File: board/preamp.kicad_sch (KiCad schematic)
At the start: 18 parts, among them U5 MAX4062

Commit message: 0.2-prototype
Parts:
- R39: value 220 -> 220-1%
- TP6: now left out of the parts list
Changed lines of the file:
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@@
 		(unit 1)
 		(exclude_from_sim no)
-		(in_bom yes)
+		(in_bom no)
 		(on_board yes)
 		(dnp no)
@@
 			)
 		)
-		(property "Value" "220"
+		(property "Value" "220-1%"
 			(at 222.25 85.09 90)
 			(effects

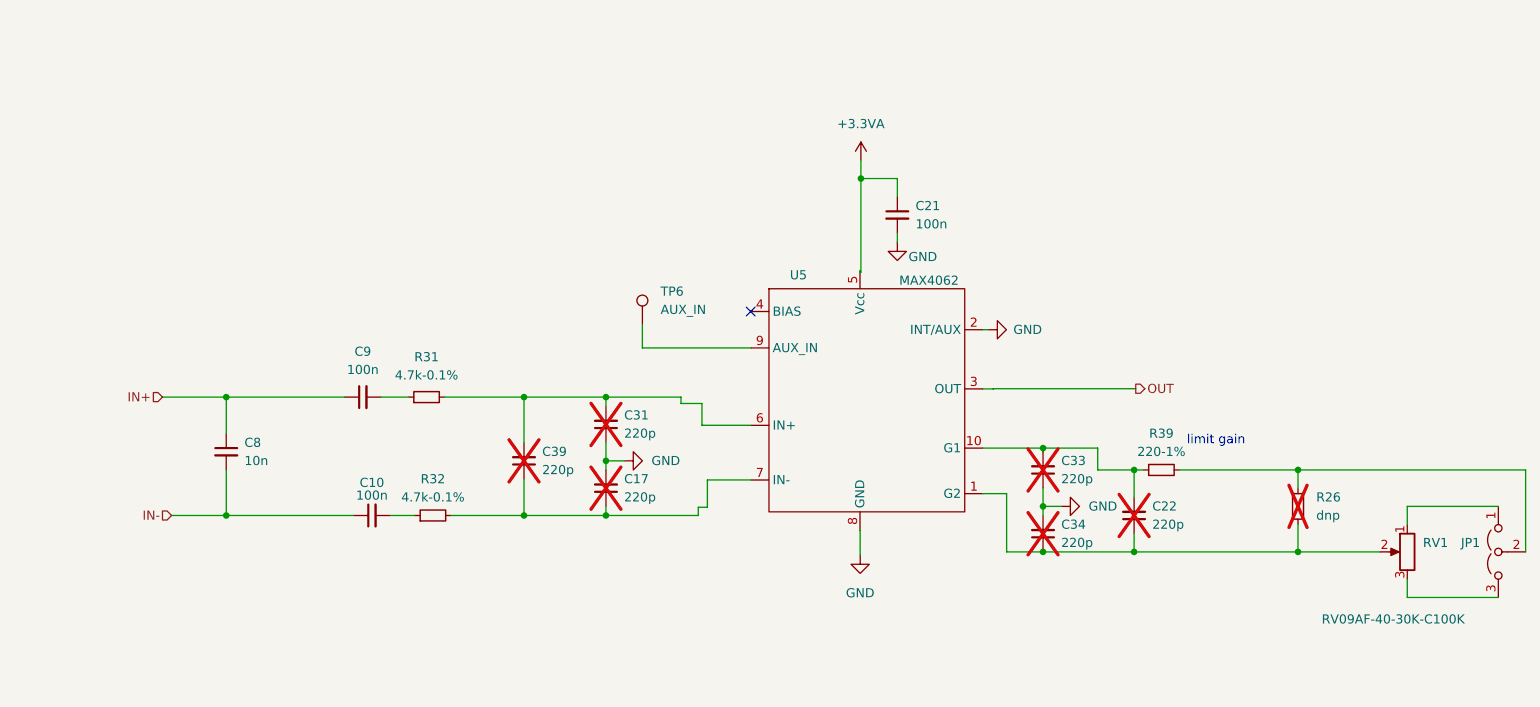
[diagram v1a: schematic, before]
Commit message: redesigned MAX section with shorter traces, analog GND plane,...
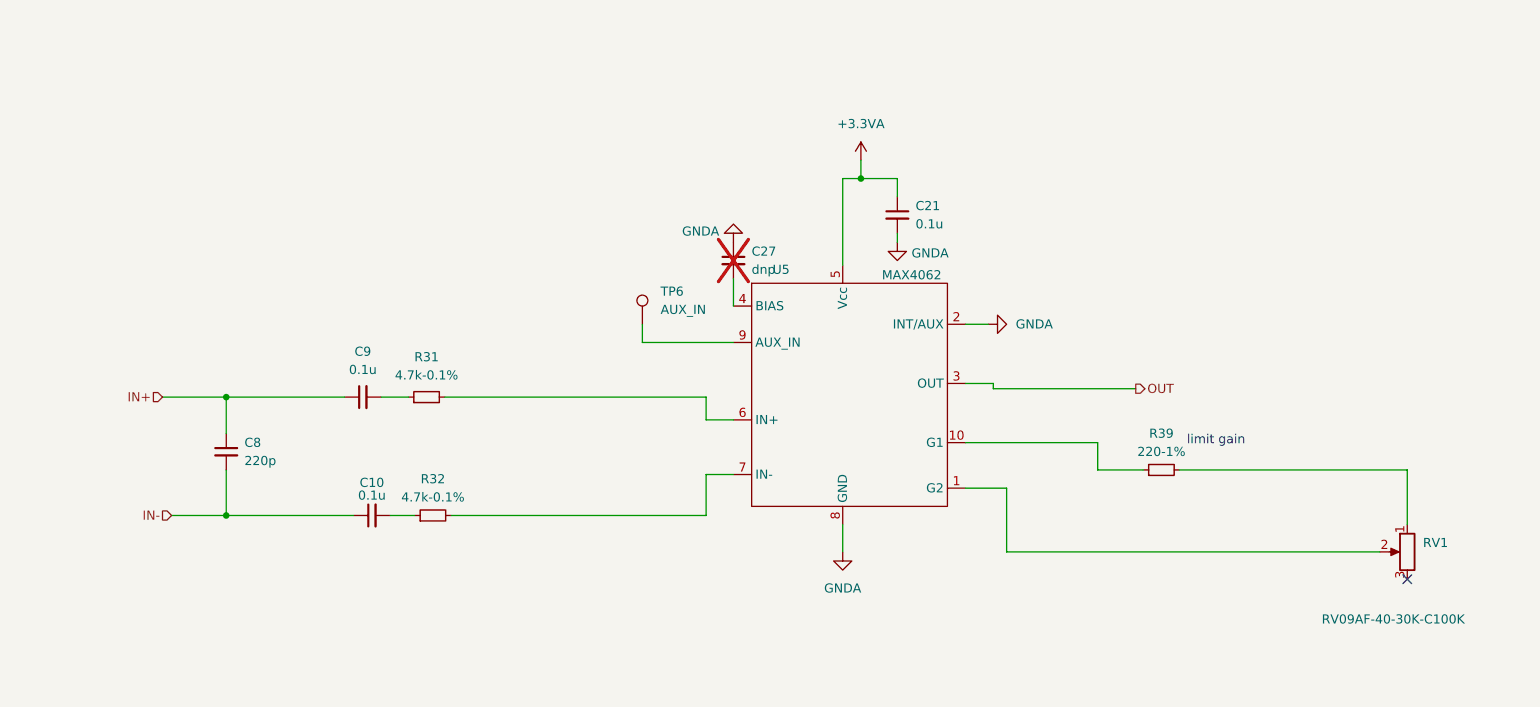
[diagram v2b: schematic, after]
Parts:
- removed C17, C22, C31, C33, C34, C39: 220p, Capacitor_THT:C_Disc_D3.0mm_W2.0mm_P2.50mm, symbol Device:C_Small
- removed JP1: ~, Jumper:SolderJumper-3_P1.3mm_Open_RoundedPad1.0x1.5mm_NumberLabels, symbol Jumper:Jumper_3_Open
- removed R26: dnp, Resistor_THT:R_Axial_DIN0207_L6.3mm_D2.5mm_P10.16mm_Horizontal, symbol Device:R_Small
- added C27: dnp, Capacitor_SMD:C_1206_3216Metric_Pad1.33x1.80mm_HandSolder, symbol Device:C_Small
- C10, C21, C9: value 100n -> 0.1u
- C8: value 10n -> 220p; footprint Capacitor_THT:C_Disc_D5.1mm_W3.2mm_P5.00mm -> Capacitor_THT:C_Disc_D3.0mm_W2.0mm_P2.50mm
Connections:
- net at R39.2: now also RV1.1
- net at U5.4 (BIAS): now also C27.2
- net GND renamed GNDA
- net GNDA: now also C27.1
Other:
- moved on the sheet: U5

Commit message: revert separating ground planes
maybe it leads to more issues than it solves
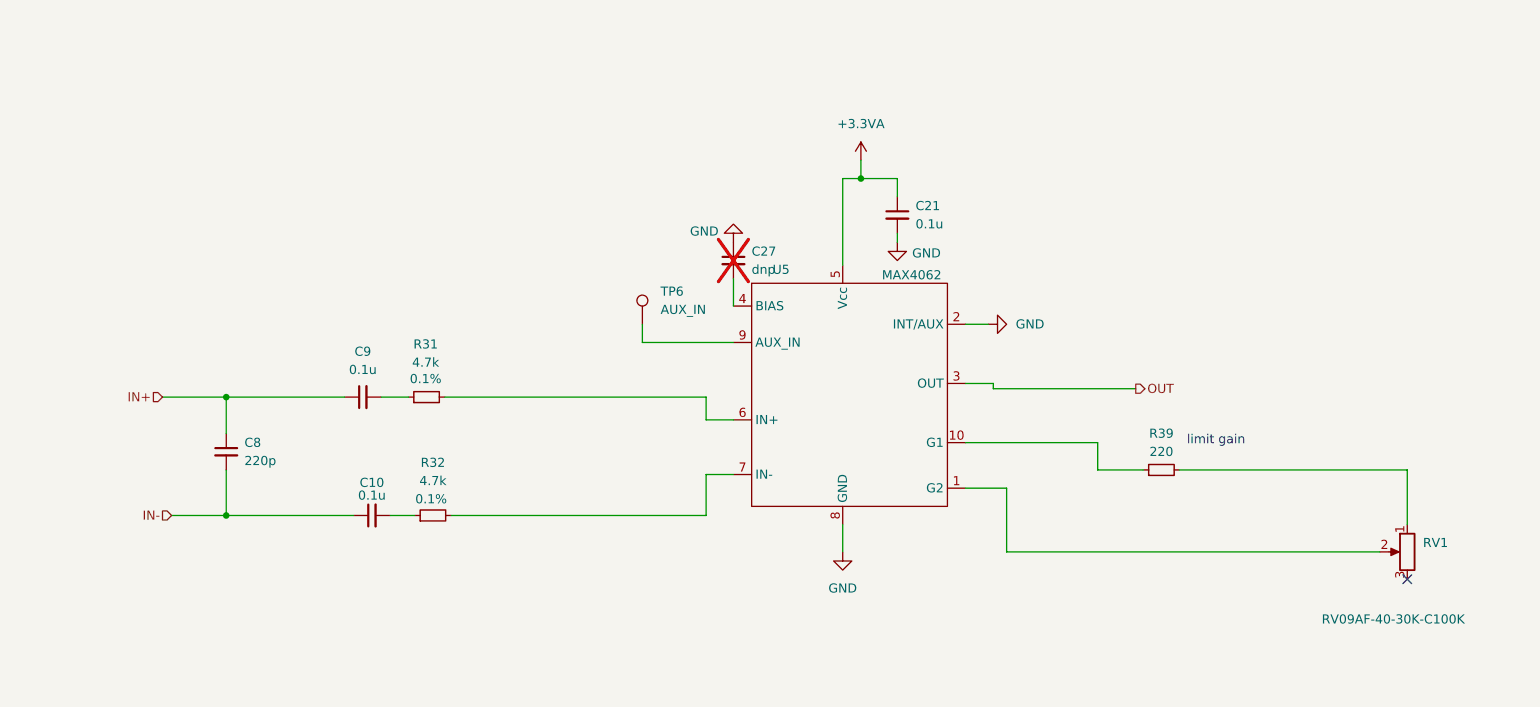
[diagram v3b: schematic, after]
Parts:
- R31, R32: value 4.7k-0.1% -> 4.7k; Note (none) -> 0.1%
- R39: value 220-1% -> 220
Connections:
- net GNDA renamed GND

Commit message: shorter traces + silkscreen updates
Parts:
- R31, R32: footprint Resistor_THT:R_Axial_DIN0207_L6.3mm_D2.5mm_P10.16mm_Horizontal -> Resistor_THT:R_Axial_DIN0207_L6.3mm_D2.5mm_P7.62mm_Horizontal
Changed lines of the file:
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@@
 			)
 		)
-		(property "Footprint" "Resistor_THT:R_Axial_DIN0207_L6.3mm_D2.5mm_P10.16mm_Horizontal"
+		(property "Footprint" "Resistor_THT:R_Axial_DIN0207_L6.3mm_D2.5mm_P7.62mm_Horizontal"
 			(at 120.65 93.98 0)
 			(effects
@@
 			)
 		)
-		(property "Footprint" "Resistor_THT:R_Axial_DIN0207_L6.3mm_D2.5mm_P10.16mm_Horizontal"
+		(property "Footprint" "Resistor_THT:R_Axial_DIN0207_L6.3mm_D2.5mm_P7.62mm_Horizontal"
 			(at 119.761 77.47 0)
 			(effects

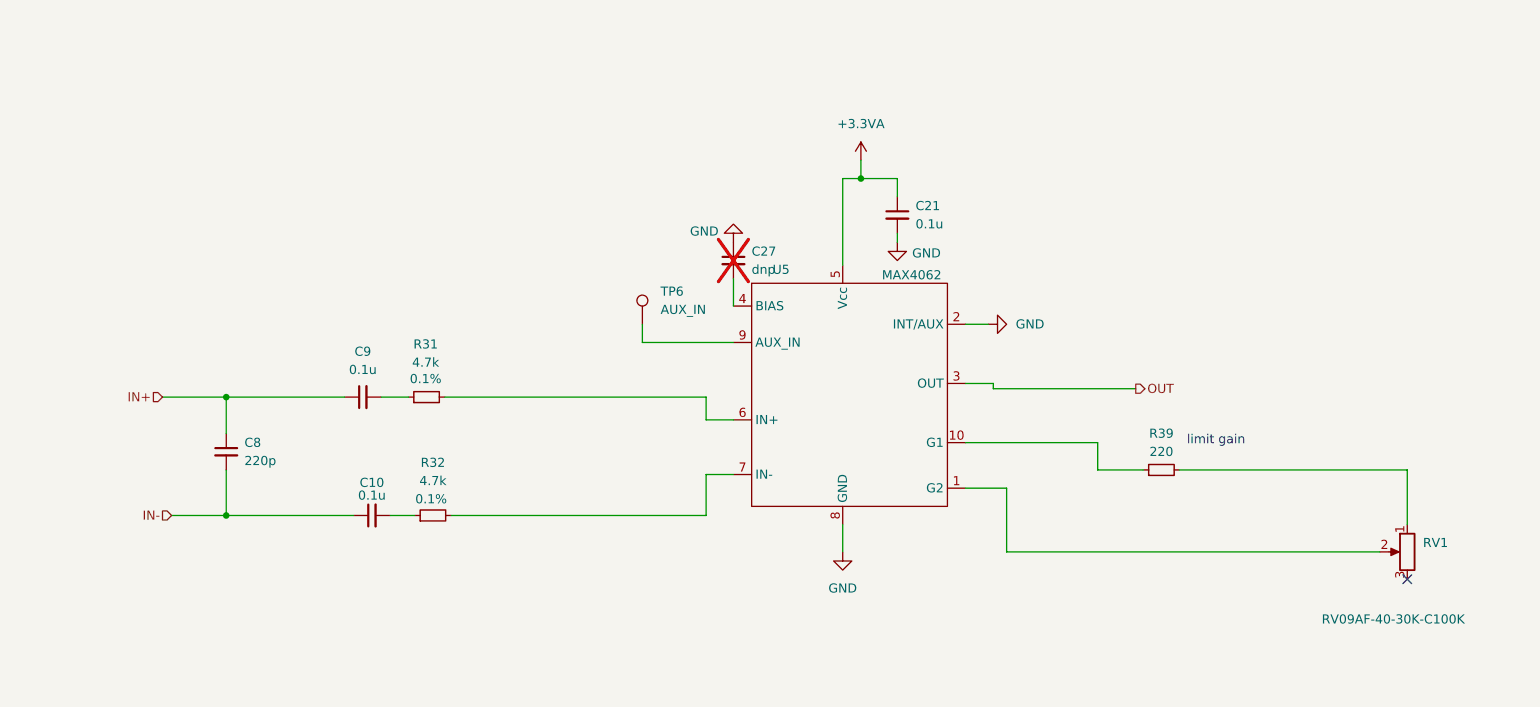
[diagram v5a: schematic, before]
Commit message: version 1.1
- replace MAX4062 with own preamplifier circuit in order to avoid difficult TSOP soldering
- easier solderable USB-C port
- add linear regulator for stable 1.65V
- replace LM358 with rail-to-rail and 3.3V compatible OPA2310 op amp
- rounded corners
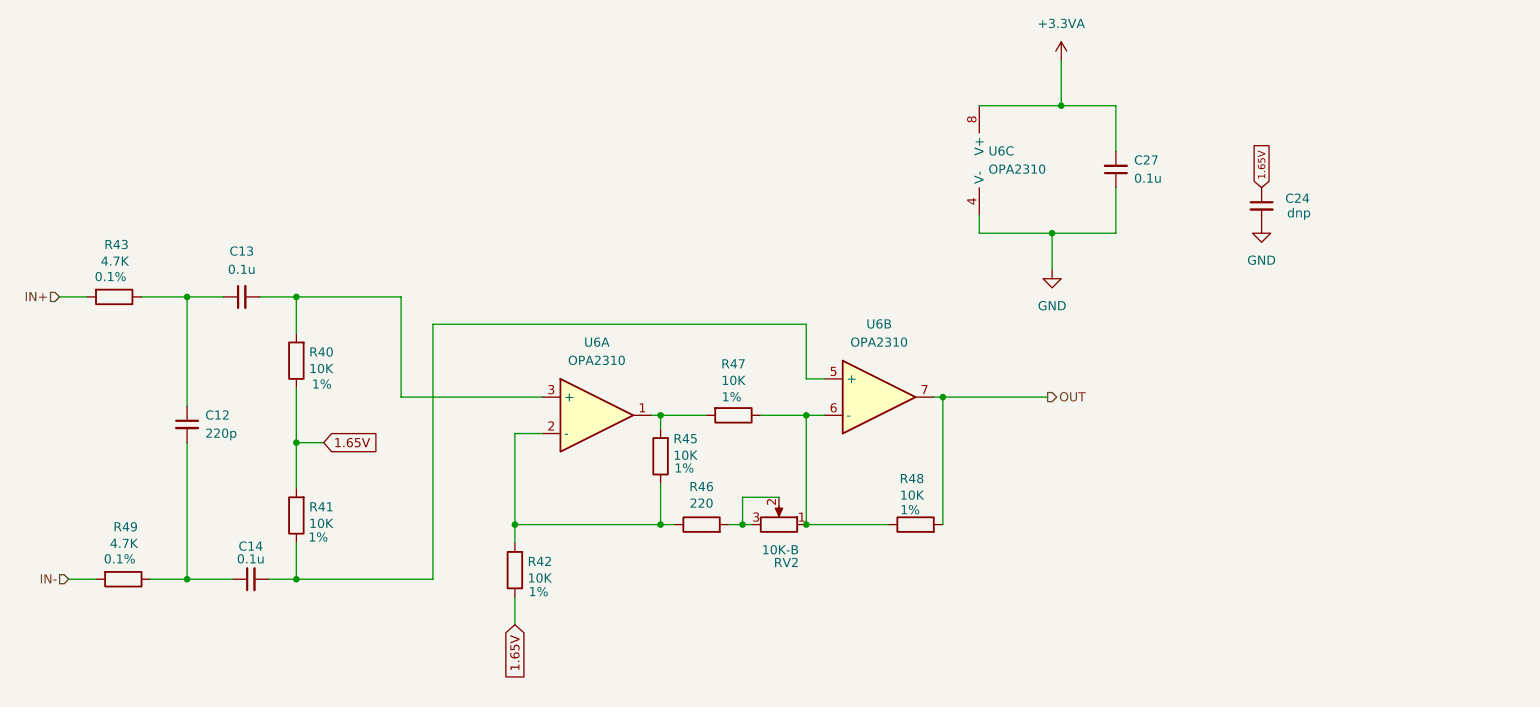
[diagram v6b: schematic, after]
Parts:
- removed C21: 0.1u, Capacitor_THT:C_Disc_D4.3mm_W1.9mm_P5.00mm, symbol Device:C_Small
- removed R31, R32: 4.7k, Resistor_THT:R_Axial_DIN0207_L6.3mm_D2.5mm_P7.62mm_Horizontal, symbol Device:R_Small
- removed R39: 220, Resistor_THT:R_Axial_DIN0204_L3.6mm_D1.6mm_P5.08mm_Horizontal, symbol Device:R_Small
- removed TP6: AUX_IN, TestPoint:TestPoint_Pad_D1.0mm, symbol Connector:TestPoint
- removed U5: MAX4062, Package_SO:MSOP-10_3x3mm_P0.5mm, symbol custom:MAX4062
- added C24: dnp, Capacitor_THT:C_Disc_D4.3mm_W1.9mm_P5.00mm, symbol Device:C_Small
- added R40, R41, R42, R45, R47, R48: 10K, Resistor_THT:R_Axial_DIN0204_L3.6mm_D1.6mm_P5.08mm_Horizontal, symbol Device:R
- added R43, R49: 4.7K, Resistor_THT:R_Axial_DIN0204_L3.6mm_D1.6mm_P5.08mm_Horizontal, symbol Device:R
- added R46: 220, Resistor_THT:R_Axial_DIN0204_L3.6mm_D1.6mm_P5.08mm_Horizontal, symbol Device:R
- added U6: OPA2310, Package_SO:SOIC-8_3.9x4.9mm_P1.27mm, symbol Device:Opamp_Dual
- C27: value dnp -> 0.1u; footprint Capacitor_SMD:C_1206_3216Metric_Pad1.33x1.80mm_HandSolder -> Capacitor_THT:C_Disc_D4.3mm_W1.9mm_P5.00mm; now fitted
- RV2: renamed from RV1; value RV09AF-40-30K-C100K -> 10K-B
- renumbered C8 to C12, C9 to C13, C10 to C14
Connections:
- net +3.3VA: now also C27.2, U6.8 (V+)
- net GND: now also C24.2, U6.4 (V-)
- net IN+: now also R43.2; no longer C12.1, C13.1
- net IN-: now also R49.2; no longer C12.2, C14.1
- net OUT: now also R48.2, U6.7
- net at RV2.1: now also R47.1, R48.1, U6.6 (-)
- net at RV2.2: now also RV2.3, R46.2
- net at C14.2: now also R41.1, U6.5 (+)
- net at C13.2: now also R40.2, U6.3 (+)
- new net: R42.2, R45.1, R46.1, U6.2 (-)
- new net: R45.2, R47.2, U6.1
- new net: C12.2, C14.1, R49.1
- new net: C12.1, C13.1, R43.1
- new net 1.65V: C24.1, R40.1, R41.2, R42.1
- no-connect marks 1 -> 0
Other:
- note removed: "limit gain"
- moved on the sheet: C12, C13, C14, RV2

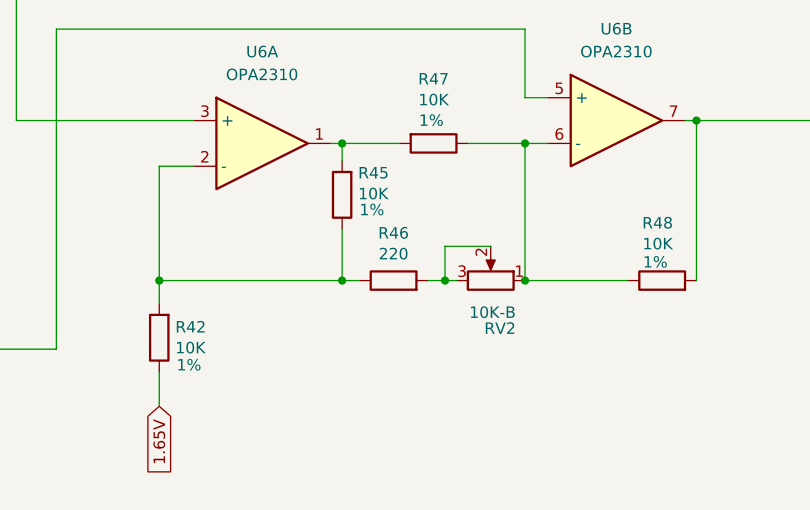
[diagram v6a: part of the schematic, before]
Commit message: version 1.1b
almost identical to 1.1, but
- Limit Microphone Gain (R36,R46)
- Battery fuse
- More room for soldering USB port
- Correct footprints for 0.1uF capacitors
- Correct footprints for 4.7k resistor
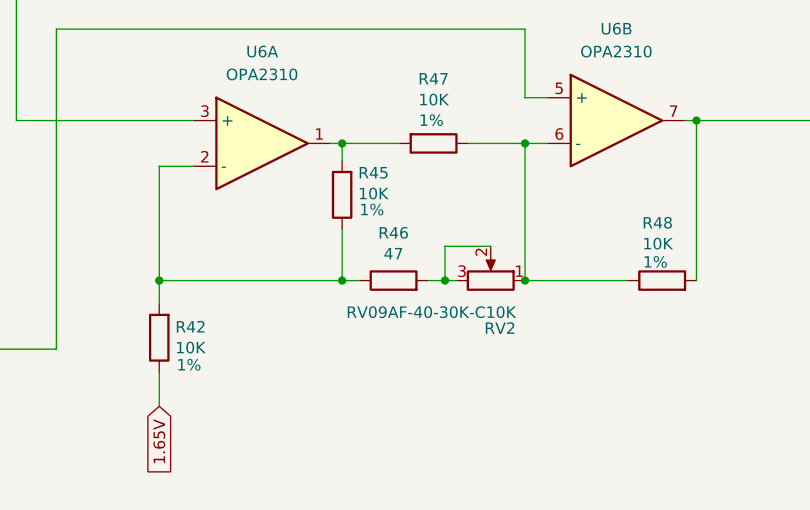
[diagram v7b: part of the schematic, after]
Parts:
- C13, C14, C24, C27: footprint Capacitor_THT:C_Disc_D4.3mm_W1.9mm_P5.00mm -> Capacitor_THT:C_Disc_D3.0mm_W2.0mm_P2.50mm
- R43, R49: footprint Resistor_THT:R_Axial_DIN0204_L3.6mm_D1.6mm_P5.08mm_Horizontal -> Resistor_THT:R_Axial_DIN0207_L6.3mm_D2.5mm_P7.62mm_Horizontal
- R46: value 220 -> 47
- RV2: value 10K-B -> RV09AF-40-30K-C10K
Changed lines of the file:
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@@
+			)
+		)
+		(property "Test" ""
+			(at 152.4 85.725 0)
+			(effects
+				(font
+					(size 1.27 1.27)
+				)
+				(hide yes)
 			)
 		)
@@
 			)
 		)
-		(property "Value" "10K-B"
+		(property "Value" "RV09AF-40-30K-C10K"
 			(at 171.704 98.806 90)
 			(effects
@@
 					(size 1.27 1.27)
 				)
+			)
+		)
+		(property "Test" ""
+			(at 168.91 95.25 0)
+			(effects
+				(font
+					(size 1.27 1.27)
+				)
+				(hide yes)
 			)
 		)
@@
 			)
 		)
-		(property "Value" "220"
+		(property "Value" "47"
 			(at 158.115 92.3036 90)
 			(effects
@@
 		)
 		(property "Description" ""
+			(at 158.115 95.25 0)
+			(effects
+				(font
+					(size 1.27 1.27)
+				)
+				(hide yes)
+			)
+		)
+		(property "Test" ""
 			(at 158.115 95.25 0)
 			(effects
@@
 			)
 		)
+		(property "Test" ""
+			(at 162.56 80.01 0)
+			(effects
+				(font
+					(size 1.27 1.27)
+				)
+				(hide yes)
+			)
+		)
 		(pin "1"
 		)
@@
 			)
 		)
+		(property "Test" ""
+			(at 143.51 80.01 0)
+			(effects
+				(font
+					(size 1.27 1.27)
+				)
+				(hide yes)
+			)
+		)
 		(pin "8"
 		)
@@
 			)
 		)
+		(property "Test" ""
+			(at 101.6 93.98 0)
+			(effects
+				(font
+					(size 1.27 1.27)
+				)
+				(hide yes)
+			)
+		)
 		(pin "1"
 		)
@@
 			)
 		)
+		(property "Test" ""
+			(at 101.6 72.39 0)
+			(effects
+				(font
+					(size 1.27 1.27)
+				)
+				(hide yes)
+			)
+		)
 		(pin "2"
 		)
@@
 			)
 		)
+		(property "Test" ""
+			(at 187.96 95.25 0)
+			(effects
+				(font
+					(size 1.27 1.27)
+				)
+				(hide yes)
+			)
+		)
 		(pin "2"
 		)
@@
 			)
 		)
-		(property "Footprint" "Capacitor_THT:C_Disc_D4.3mm_W1.9mm_P5.00mm"
+		(property "Footprint" "Capacitor_THT:C_Disc_D3.0mm_W2.0mm_P2.50mm"
 			(at 95.25 102.87 0)
 			(effects
@@
 		)
 		(property "Sim.Type" ""
+			(at 95.25 102.87 0)
+			(effects
+				(font
+					(size 1.27 1.27)
+				)
+				(hide yes)
+			)
+		)
+		(property "Test" ""
 			(at 95.25 102.87 0)
 			(effects
@@
 			)
 		)
-		(property "Footprint" "Capacitor_THT:C_Disc_D4.3mm_W1.9mm_P5.00mm"
+		(property "Footprint" "Capacitor_THT:C_Disc_D3.0mm_W2.0mm_P2.50mm"
 			(at 236.22 50.8 0)
 			(effects
@@
 					(size 1.27 1.27)
 				)
+			)
+		)
+		(property "Test" ""
+			(at 236.22 50.8 0)
+			(effects
+				(font
+					(size 1.27 1.27)
+				)
+				(hide yes)
 			)
 		)
@@
 			)
 		)
-		(property "Footprint" "Capacitor_THT:C_Disc_D4.3mm_W1.9mm_P5.00mm"
+		(property "Footprint" "Capacitor_THT:C_Disc_D3.0mm_W2.0mm_P2.50mm"
 			(at 93.98 63.5 0)
 			(effects
@@
 		)
 		(property "Sim.Type" ""
+			(at 93.98 63.5 0)
+			(effects
+				(font
+					(size 1.27 1.27)
+				)
+				(hide yes)
+			)
+		)
+		(property "Test" ""
 			(at 93.98 63.5 0)
 			(effects
@@
 			)
 		)
+		(property "Test" ""
+			(at 182.88 77.47 0)
+			(effects
+				(font
+					(size 1.27 1.27)
+				)
+				(hide yes)
+			)
+		)
 		(pin "8"
 		)
@@
 			)
 		)
+		(property "Test" ""
+			(at 132.08 101.6 0)
+			(effects
+				(font
+					(size 1.27 1.27)
+				)
+				(hide yes)
+			)
+		)
 		(pin "2"
 		)
@@
 			)
 		)
-		(property "Footprint" "Resistor_THT:R_Axial_DIN0204_L3.6mm_D1.6mm_P5.08mm_Horizontal"
+		(property "Footprint" "Resistor_THT:R_Axial_DIN0207_L6.3mm_D2.5mm_P7.62mm_Horizontal"
 			(at 76.2 61.722 90)
 			(effects
@@
 					(size 1.27 1.27)
 				)
+			)
+		)
+		(property "Test" ""
+			(at 76.2 63.5 0)
+			(effects
+				(font
+					(size 1.27 1.27)
+				)
+				(hide yes)
 			)
 		)
@@
 			)
 		)
-		(property "Footprint" "Capacitor_THT:C_Disc_D4.3mm_W1.9mm_P5.00mm"
+		(property "Footprint" "Capacitor_THT:C_Disc_D3.0mm_W2.0mm_P2.50mm"
 			(at 215.9 45.72 0)
 			(effects
@@
 		)
 		(property "Sim.Type" ""
+			(at 215.9 45.72 0)
+			(effects
+				(font
+					(size 1.27 1.27)
+				)
+				(hide yes)
+			)
+		)
+		(property "Test" ""
 			(at 215.9 45.72 0)
 			(effects
@@
 			)
 		)
+		(property "Test" ""
+			(at 199.39 44.45 0)
+			(effects
+				(font
+					(size 1.27 1.27)
+				)
+				(hide yes)
+			)
+		)
 		(pin "8"
 		)
@@
 			)
 		)
+		(property "Test" ""
+			(at 86.36 81.28 0)
+			(effects
+				(font
+					(size 1.27 1.27)
+				)
+				(hide yes)
+			)
+		)
 		(pin "1"
 		)
@@
 			)
 		)
-		(property "Footprint" "Resistor_THT:R_Axial_DIN0204_L3.6mm_D1.6mm_P5.08mm_Horizontal"
+		(property "Footprint" "Resistor_THT:R_Axial_DIN0207_L6.3mm_D2.5mm_P7.62mm_Horizontal"
 			(at 77.47 101.092 90)
 			(effects
@@
 			)
 		)
+		(property "Test" ""
+			(at 77.47 102.87 0)
+			(effects
+				(font
+					(size 1.27 1.27)
+				)
+				(hide yes)
+			)
+		)
